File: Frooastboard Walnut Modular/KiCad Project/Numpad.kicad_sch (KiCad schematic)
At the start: 73 parts, among them M2 Frooastboard_MM2040

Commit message: idk some updates
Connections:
- no-connect marks 19 -> 21
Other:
- moved on the sheet: C40, R29, R30, R31, USB3

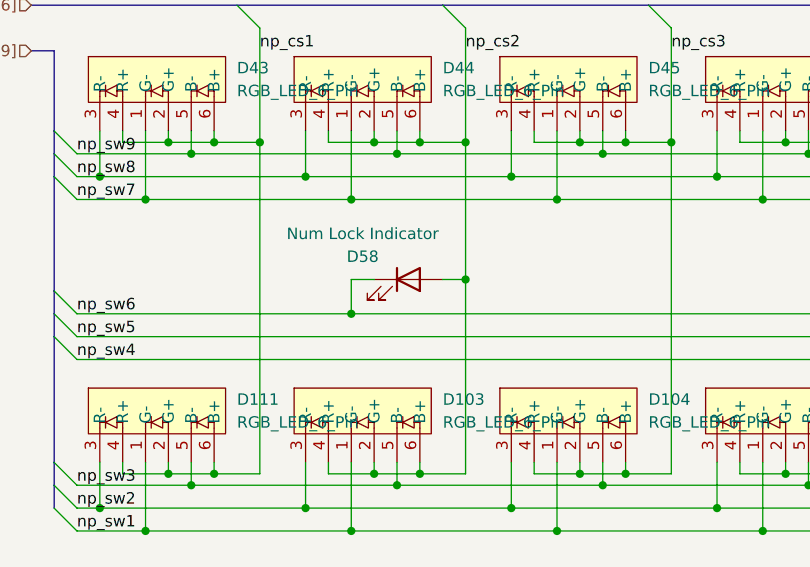
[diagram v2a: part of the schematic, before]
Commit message: update leds and diodes
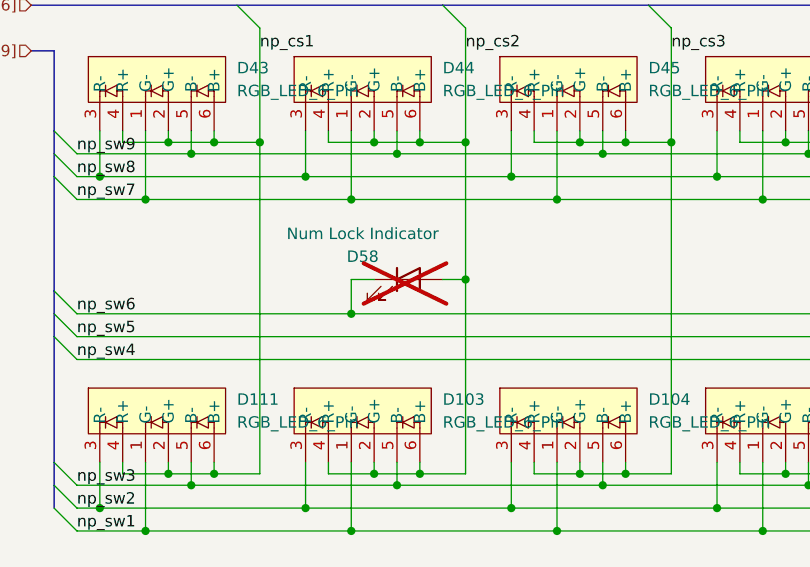
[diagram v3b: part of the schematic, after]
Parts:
- D58: now not fitted; now left out of the parts list
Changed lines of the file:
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@@
   )
   (symbol (lib_id "Device:LED") (at 68.58 58.42 0) (unit 1)
-    (in_bom yes) (on_board yes) (dnp no)
+    (in_bom no) (on_board no) (dnp yes)
     (property "Reference" "D58" (at 63.5 55.88 0)
       (effects (font (size 1.27 1.27)))

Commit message: some stuff
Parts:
- MX35: footprint MX_Only:MXOnly-2U-ReversedVerticalStabilizers-NoLED -> MX_Only:MXOnly-2U-NoLED
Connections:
- net np_dn renamed np_d-
- net np_dp renamed np_d+
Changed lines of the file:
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@@
     (effects (font (size 1.27 1.27)) (justify right))
   )
-  (hierarchical_label "np_dn" (shape bidirectional) (at 234.95 132.08 0) (fields_autoplaced)
+  (hierarchical_label "np_d-" (shape bidirectional) (at 234.95 132.08 0) (fields_autoplaced)
     (effects (font (size 1.27 1.27)) (justify left))
   )
@@
     (effects (font (size 1.27 1.27)) (justify left))
   )
-  (hierarchical_label "np_dp" (shape bidirectional) (at 313.69 173.99 180) (fields_autoplaced)
+  (hierarchical_label "np_d+" (shape bidirectional) (at 313.69 173.99 180) (fields_autoplaced)
     (effects (font (size 1.27 1.27)) (justify right))
   )
@@
     (effects (font (size 1.27 1.27)) (justify right))
   )
-  (hierarchical_label "np_dn" (shape bidirectional) (at 313.69 171.45 180) (fields_autoplaced)
+  (hierarchical_label "np_d-" (shape bidirectional) (at 313.69 171.45 180) (fields_autoplaced)
     (effects (font (size 1.27 1.27)) (justify right))
   )
@@
     (effects (font (size 1.27 1.27)) (justify right))
   )
-  (hierarchical_label "np_dp" (shape bidirectional) (at 234.95 134.62 0) (fields_autoplaced)
+  (hierarchical_label "np_d+" (shape bidirectional) (at 234.95 134.62 0) (fields_autoplaced)
     (effects (font (size 1.27 1.27)) (justify left))
   )
@@
       (effects (font (size 0.508 0.508)))
     )
-    (property "Footprint" "MX_Only:MXOnly-2U-ReversedVerticalStabilizers-NoLED" (at 136.525 177.165 0)
-      (effects (font (size 1.524 1.524)) hide)
-    )
+    (property "Footprint" "MX_Only:MXOnly-2U-NoLED" (at 136.525 177.165 0)
+      (effects (font (size 1.524 1.524)) hide)
+    )

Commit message: fix errors
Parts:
- MX32: value Comma -> Dot
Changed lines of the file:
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@@
       (effects (font (size 1.524 1.524)))
     )
-    (property "Value" "Comma" (at 144.3956 222.25 0)
+    (property "Value" "Dot" (at 144.3956 222.25 0)
       (effects (font (size 0.508 0.508)))
     )
